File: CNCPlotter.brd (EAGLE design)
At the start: 172.4 x 76.8 mm, 125 parts, among them IC1 HEF4050B, IC2 MC34063, IC3 LD1117S33, IC4 74HC4094, IC5 ATmega32U4, IC6 DRV8811, IC7 DRV8811, J1 Home Switches, J10 ISP, J11 X Motor, J12 MS1, J13 MS0, J14 Y Motor, J15 MS1, J16 MS0, J2 Touchscreen, J3 12V Supply, J4 MicroSD Card, J5 HWB, J6 USB-FT, J7 Servo, J8 Z Drive, J9 UART, Q1 16MHz

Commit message: foo
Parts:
- added J17: MS0, freetronics-luke:SJ
- C1, C13, C25: value 100 uF -> 100uF
- C10, C7, C8: value 100nF -> 100 nF; device freetronics:0603 -> freetronics-master-v1:0603
- C11, C12: device freetronics:0603 -> freetronics-master-v1:0603
- C17, C18, C29, C30: value 680 pF -> 1nF
- C9: value 1uF -> 1 uF; device freetronics:0603 -> freetronics-master-v1:0603
- F1: value 500mA PPTC -> 500mA
- J1: value Home Switches -> Servo; device con-molex:22-23-2061 -> con-molex:22-23-2031
- J10: value ISP -> Touchscreen; device SparkFun:2X3-NS -> pinhead:1X04
- J11: value X Motor -> Touchscreen; device con-phoenix-254:4POL254 -> SparkFun:DS_TOUCH_CONNECTOR
- J12: value MS1 -> X Motor; device freetronics-luke:SJ -> con-phoenix-254:4POL254
- J13, J16: value MS0 -> MS1
- J14: value Y Motor -> MS0; device con-phoenix-254:4POL254 -> freetronics-luke:SJ
- J15: value MS1 -> Y Motor; device freetronics-luke:SJ -> con-phoenix-254:4POL254
- J2: value Touchscreen -> Z Drive; device SparkFun:DS_TOUCH_CONNECTOR -> con-phoenix-254:5POL254
- J3: value 12V Supply -> ISP; device SparkFun:POWER_JACK_SLOT -> SparkFun:2X3-NS
- J4: value MicroSD Card -> UART; device RAMPSdisplay:ADAFRUIT_MICROSD -> pinhead:1X04
- J5: value HWB -> 12V Supply; device freetronics-luke:SJ -> SparkFun:POWER_JACK_SLOT
- J6: value USB-FT -> MicroSD Card; device freetronics-luke:USB-MINIB-FT -> RAMPSdisplay:ADAFRUIT_MICROSD
- J7: value Servo -> HWB; device con-molex:22-23-2031 -> freetronics-luke:SJ
- J8: value Z Drive -> USB-FT; device con-molex:22-23-2051 -> freetronics-luke:USB-MINIB-FT
- J9: value UART -> Home Switches; device con-molex:22-23-2041 -> con-phoenix-254:6POL254
- LED1: value TXD -> TX
- LED2: value RXD -> RX
- LED4: value Z Home -> Z
- LED5: value Y Home -> Y
- LED6: value X Home -> X
- LED7: value 12V -> 12
- R10: value 10k -> 3k0
- R11: value 0.2 ohms -> 1k; device rcl:R1210 -> freetronics-master-v1:0603
- R12: value 1k -> 22R
- R13: value 3k0 -> 10k
- R14: value 1k -> 10k
- R16: value 10k -> 22R
- R18, R19: value 22R -> 10k
- R20, R21, R22, R23, R25, R30, R31: value 10k -> 10K
- R24: value 3k3 -> 3K3
- R26, R27, R40, R41: value 56k -> 47K
- R29, R43: value 4k7 -> 4K7
- R32, R33: value 0.2R 1W -> 0.25R 1W
- R8: value 10k -> 0.2 ohms; device freetronics-master-v1:0603 -> rcl:R1210
- R9: value 10k -> 1k
- VR2: value 10 k -> 10K
- moved J2 79.3 mm to (54.6, 67.9), turned to 180 degrees
- moved J5 78.6 mm to (6.35, 63.5), turned to 180 degrees
- moved LED8 78.2 mm to (1.75, 28.4), turned to 180 degrees
- moved R11 73.6 mm to (4.76, 28.4)
- moved J8 71.9 mm to (17.1, 67.3), turned to 270 degrees
- moved C3 71.9 mm to (12.7, 55.9), turned to 180 degrees
- moved C6 71.5 mm to (12.1, 25.4)
- moved J1 71.5 mm to (80.0, 67.9), turned to 180 degrees
- moved C5 70.4 mm to (10.8, 12.1)
- moved D1 69.5 mm to (12.1, 16.5), turned to 90 degrees
- moved J9 68.4 mm to (38.1, 67.9), turned to 180 degrees
- moved C2 67.6 mm to (13.3, 22.2), turned to 180 degrees
- moved C25 65.8 mm to (100.3, 57.1)
- moved R16 63.3 mm to (19.2, 54.6), turned to 180 degrees
- moved Z1 62.7 mm to (19.1, 57.1), turned to 90 degrees
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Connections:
- new net N$71: R42.2, VR3.A
- net !RESET: now also J3.5, R14.1; no longer J10.5, R17.1
- net !SD_CS: now also R13.1; no longer R16.1
- net +12V: now also J2.1, J5.PWR, R8.1; no longer J3.PWR, J8.1, R11.1
- net +5V: now also J1.2, J2.3, J3.2, J4.1, J9.3, J9.5, R12.2, R13.2, R14.2; no longer J1.1, J1.3, J1.5, J10.2, J7.2, J8.3, R15.2, R16.2, R17.2
- net FOO: now also J6.2; no longer J4.2
- net GND: now also C7.2, J1.1, J14.1, J17.1, J2.2, J3.6, J4.2, J5.GND, J6.6, J6.MT1, J6.MT2, J8.GND, J8.SH1, J8.SH2, J8.SH3, J8.SH4, R17.2, R18.2, R19.2; no longer C7.1, J10.6, J12.1, J15.1, J3.GND@1, J4.6, J4.MT1, J4.MT2, J5.1, J6.GND, J6.SH1, J6.SH2, J6.SH3, J6.SH4, J8.2, J9.2, R10.2, R12.2, R8.2
- net HWB: now also J7.2; no longer J5.2
- net MISO: now also J3.1, J6.7; no longer J10.1, J4.7
- net MOSI: now also J3.4; no longer J10.4
- net MOSI_3.3V: now also J6.3; no longer J4.3
- net N$1: now also J15.1; no longer J14.1
- net N$2: now also J8.VBUS; no longer J6.VBUS
- net N$20: no longer R42.2, VR3.A
- net N$21: now also J12.4; no longer J11.4
- net N$22: now also J12.3; no longer J11.3
- net N$23: now also J12.2; no longer J11.2
- net N$3: now also J12.1; no longer J11.1
- net N$32: now also R8.2; no longer R11.2
- net N$33: now also J8.D+, R16.2; no longer J6.D+, R19.2
- net N$34: now also J8.D-, R15.2; no longer J6.D-, R18.2
- net N$37: now also R16.1; no longer R19.1
- net N$38: now also R15.1; no longer R18.1
- net N$4: now also J15.4; no longer J14.4
- net N$40: now also C7.1; no longer C7.2
- net N$44: now also R10.2, R9.1; no longer R12.1, R13.2
- net N$5: now also J15.3; no longer J14.3
- net N$59: now also R12.1; no longer R15.1
- net N$6: now also J15.2; no longer J14.2
- net N$62: now also R11.1; no longer R14.1
- net N$63: now also R11.2; no longer R14.2
- net N$66: now also J13.2; no longer J12.2
- net N$67: now also J14.2; no longer J13.2
- net N$74: now also J16.2; no longer J15.2
- net N$75: now also J17.2; no longer J16.2
- net REG_5V: now also R10.1; no longer R13.1
- net RXD: now also J4.3; no longer J9.3
- net SCK: now also J3.3; no longer J10.3
- net SCK_3.3V: now also J6.5; no longer J4.5
- net SERVO: now also J1.3; no longer J7.3
- net TOUCH1: now also J10.1, J11.Y1; no longer J2.Y1
- net TOUCH2: now also J10.2, J11.X2; no longer J2.X2
- net TOUCH3: now also J10.3, J11.Y2; no longer J2.Y2
- net TOUCH4: now also J10.4, J11.X1; no longer J2.X1
- net TXD: now also J4.4; no longer J9.4
- net VDD: now also J6.4; no longer J4.4
- net X_HOME: now also J9.2, R17.1; no longer J1.2, R8.1
- net Y_HOME: now also J9.4, R18.1; no longer J1.4, R9.1
- net Z_DIR: now also J2.4; no longer J8.4
- net Z_HOME: now also J9.6, R19.1; no longer J1.6, R10.1
- net Z_STEP: now also J2.5; no longer J8.5
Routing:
- net +5V: track 0.00 -> 445.8 mm, vias 0 -> 24
- net +12V: track 0.00 -> 244.9 mm, vias 0 -> 12
- net X_STEP: track 0.00 -> 222.4 mm, vias 0 -> 8
- net Y_STEP: track 0.00 -> 159.8 mm, vias 0 -> 14
- net Z_HOME: track 0.00 -> 149.3 mm, vias 0 -> 4
- net Y_HOME: track 0.00 -> 148.2 mm, vias 0 -> 4
- net SERVO: track 0.00 -> 145.6 mm, vias 0 -> 1
- net RXLED: track 0.00 -> 138.4 mm, vias 0 -> 6
- net X_HOME: track 0.00 -> 136.9 mm, vias 0 -> 6
- net !SD_CS: track 0.00 -> 106.9 mm, vias 0 -> 5
- net MISO: track 0.00 -> 102.9 mm, vias 0 -> 5
- net Y_DIR: track 0.00 -> 102.9 mm, vias 0 -> 3
- net Z_STEP: track 0.00 -> 101.7 mm, vias 0 -> 3
- net TXD: track 0.00 -> 97.1 mm, vias 0 -> 1
- net RXD: track 0.00 -> 96.5 mm, vias 0 -> 1
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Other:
- board size 172.4 x 76.8 mm -> 112.4 x 73.7 mm
- board text added: "+5V"
- board text added: "1"
- board text added: "12V"
- board text added: "5V"
- board text added: "Current Limit"
- board text added: "DIR"
- board text added: "GND"
- board text added: "HWB"
- board text added: "Home Switches"
- board text added: "IC5"
- board text added: "J3"
- board text added: "L1"
- board text added: "LCD Contrast"
- board text added: "PWM"
- board text added: "RXD"
- board text added: "STP"
- board text added: "TXD"
- board text added: "X"
- board text added: "XA1"
- board text added: "XA2"
- board text added: "XB1"
- board text added: "XB2"
- board text added: "Y"
- board text added: "YA1"
- board text added: "YA2"
- board text added: "YB1"
- board text added: "YB2"
- board text added: "Z"

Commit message: foo
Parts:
- R32, R33: value 0.25R 1W -> 0.20Ω 1W
- R46, R47: value 0.2R 1W -> 0.20Ω 1W
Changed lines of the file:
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@@
 <attribute name="VALUE" x="81.1784" y="6.223" size="0.8128" layer="27" ratio="15"/>
 </element>
-<element name="R32" library="rcl" package="R2010" value="0.25R 1W" x="78.105" y="49.53" smashed="yes" rot="R270">
+<element name="R32" library="rcl" package="R2010" value="0.20Ω 1W" x="78.105" y="49.53" smashed="yes" rot="R270">
 <attribute name="NAME" x="77.073125" y="49.53" size="0.8128" layer="25" ratio="15"/>
 <attribute name="VALUE" x="79.375" y="7.62" size="0.8128" layer="27" ratio="15"/>
@@
 <attribute name="VALUE" x="82.804" y="8.8773" size="0.8128" layer="27" font="vector" ratio="15"/>
 </element>
-<element name="R33" library="rcl" package="R2010" value="0.25R 1W" x="59.055" y="49.53" smashed="yes" rot="R270">
+<element name="R33" library="rcl" package="R2010" value="0.20Ω 1W" x="59.055" y="49.53" smashed="yes" rot="R270">
 <attribute name="NAME" x="58.023125" y="49.53" size="0.8128" layer="25" ratio="15"/>
 <attribute name="VALUE" x="78.105" y="7.62" size="0.8128" layer="27" ratio="15"/>
@@
 <attribute name="VALUE" x="78.0034" y="5.588" size="0.8128" layer="27" ratio="15"/>
 </element>
-<element name="R46" library="rcl" package="R2010" value="0.2R 1W" x="100.965" y="49.53" smashed="yes" rot="R270">
+<element name="R46" library="rcl" package="R2010" value="0.20Ω 1W" x="100.965" y="49.53" smashed="yes" rot="R270">
 <attribute name="NAME" x="99.85375" y="49.53" size="0.8128" layer="25" ratio="15"/>
 <attribute name="VALUE" x="79.21625" y="6.19125" size="0.8128" layer="27" ratio="15"/>
@@
 <attribute name="VALUE" x="79.3115" y="6.6548" size="0.8128" layer="27" font="vector" ratio="15"/>
 </element>
-<element name="R47" library="rcl" package="R2010" value="0.2R 1W" x="81.915" y="49.53" smashed="yes" rot="R270">
+<element name="R47" library="rcl" package="R2010" value="0.20Ω 1W" x="81.915" y="49.53" smashed="yes" rot="R270">
 <attribute name="NAME" x="80.80375" y="49.53" size="0.8128" layer="25" ratio="15"/>
 <attribute name="VALUE" x="78.74" y="6.985" size="0.8128" layer="27" ratio="15"/>
@@
 </signal>
 </signals>
-<errors>
-</errors>
 </board>
 </drawing>

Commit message: foo
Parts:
- C10, C4, C5, C7, C8: value 100 nF -> 100nF
- C2: value 47 uF -> 47µF
- C3: value 100 pF -> 100pF
- C6: value 10uF -> 10µF
- C9: value 1 uF -> 1µF
- IC3: value LD1117S33 -> LD111733
- J8: value USB-FT -> USB
- LED8: value SD act -> SD
- R8: value 0.2 ohms -> 0.2Ω
- VR1, VR3: value 10 k -> 10kΩ
- VR2: value 10K -> 10kΩ
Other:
- board text added: "+"
- board text added: "J5"
- board text removed: "Home Switches"
- board text removed: "J3"

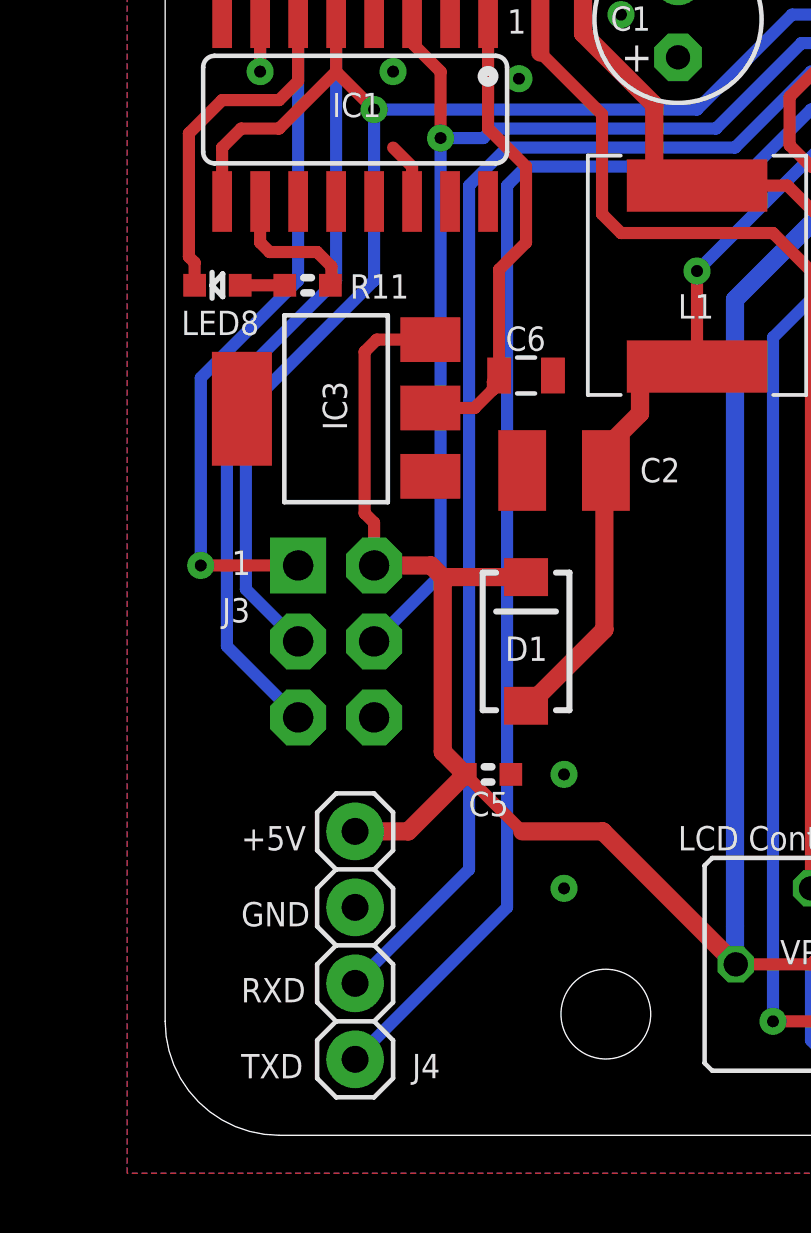
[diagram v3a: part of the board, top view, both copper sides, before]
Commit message: added reset button
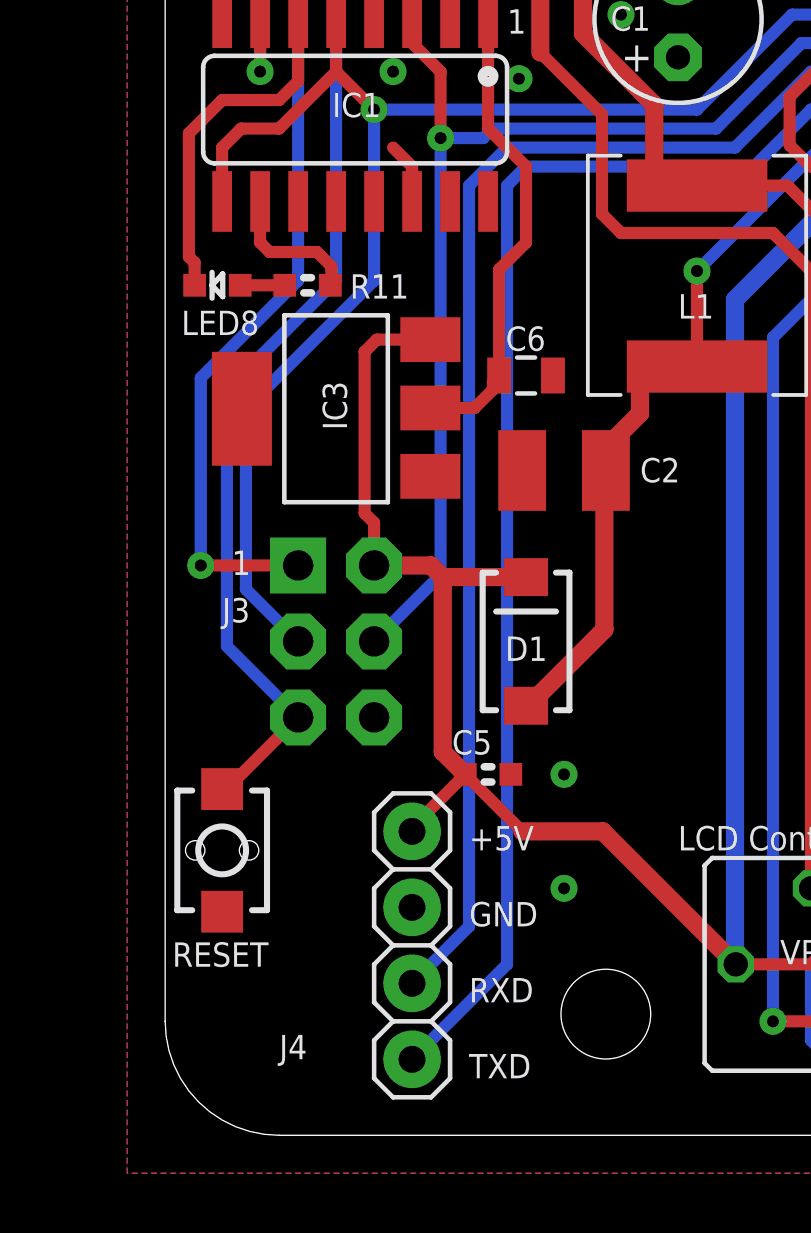
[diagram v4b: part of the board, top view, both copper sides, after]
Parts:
- added S1: RESET, freetronics-master-v1:TACTILE_SWITCH_SMD_2PIN_TINY
- moved J4 1.91 mm to (8.26, 6.35)
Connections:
- net !RESET: now also S1.2
- net GND: now also S1.1
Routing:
- net !RESET: track 84.8 -> 88.4 mm
- net +5V: track 445.8 -> 444.0 mm
- net TXD: track 97.1 -> 96.3 mm
- net RXD: track 96.5 -> 95.7 mm
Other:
- board text added: "RESET"
